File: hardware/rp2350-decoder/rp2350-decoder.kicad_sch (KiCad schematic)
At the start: 67 parts, among them J1 SWDIO, J2 SWCLK, J3 5052702412, Q1 DMN2991UDA-7B, Q2 DMN2991UDA-7B, Q3 NST847BPDP6T5G, Q4 NST847BPDP6T5G, Q5 DMN2991UDA-7B, Q6 DMN2991UDA-7B, Q7 DMN2991UDA-7B, Q8 DMN2991UDA-7B, SW1 BOOT, U1 NCS2220AMUT1G, U2 AP63203WU, U3 W25Q128JVPIQ, U4 RP2350A, U5 MAX98357AEWL+T, U6 MD9927, Y1 ABM8-272-T3

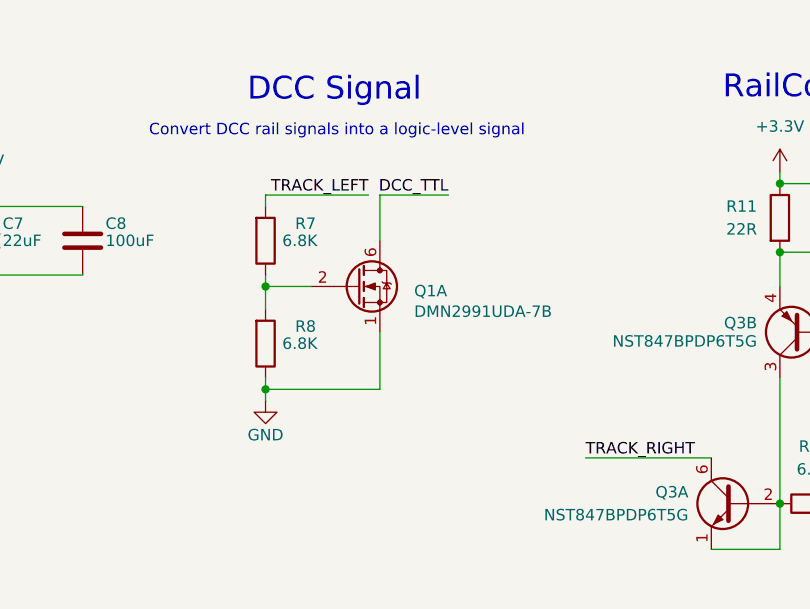
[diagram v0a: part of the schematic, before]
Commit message: fix: lower gate voltage to the dcc signal mosfet
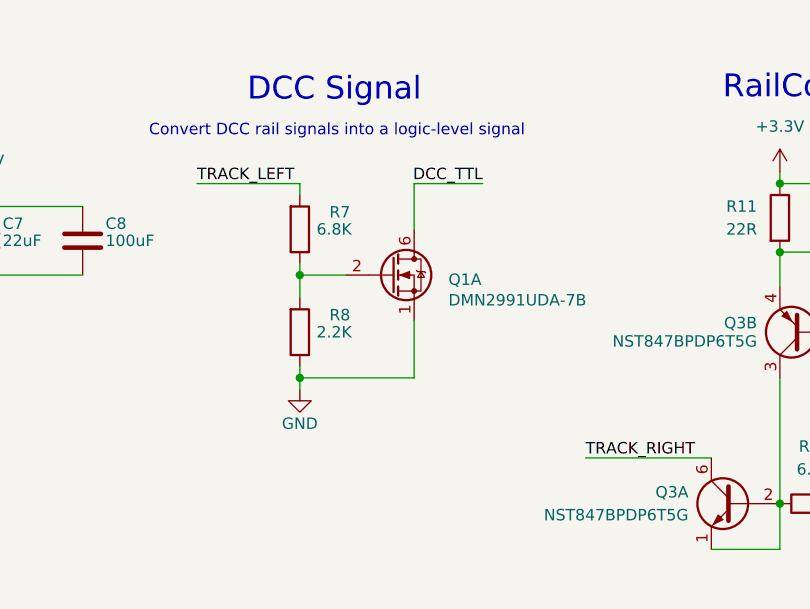
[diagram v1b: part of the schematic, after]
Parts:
- R8: value 6.8K -> 2.2K; LCSC C423451 -> C473534
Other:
- moved on the sheet: Q1A, R7, R8
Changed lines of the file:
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@@
 	)
 	(junction
-		(at 149.86 63.5)
+		(at 153.67 62.23)
 		(diameter 0)
 		(color 0 0 0 0)
@@
 	)
 	(junction
-		(at 149.86 52.07)
+		(at 153.67 50.8)
 		(diameter 0)
 		(color 0 0 0 0)
@@
 	(wire
 		(pts
-			(xy 149.86 50.8) (xy 149.86 52.07)
+			(xy 153.67 49.53) (xy 153.67 50.8)
 		)
 		(stroke
@@
 	(wire
 		(pts
-			(xy 162.56 57.15) (xy 162.56 63.5)
+			(xy 166.37 55.88) (xy 166.37 62.23)
 		)
 		(stroke
@@
 	(wire
 		(pts
-			(xy 149.86 41.91) (xy 149.86 43.18)
+			(xy 153.67 40.64) (xy 153.67 41.91)
 		)
 		(stroke
@@
 	(wire
 		(pts
-			(xy 149.86 62.23) (xy 149.86 63.5)
+			(xy 153.67 60.96) (xy 153.67 62.23)
 		)
 		(stroke
@@
 	(wire
 		(pts
-			(xy 162.56 41.91) (xy 170.18 41.91)
+			(xy 166.37 40.64) (xy 173.99 40.64)
 		)
 		(stroke
@@
 	(wire
 		(pts
-			(xy 149.86 52.07) (xy 149.86 54.61)
+			(xy 153.67 50.8) (xy 153.67 53.34)
 		)
 		(stroke
@@
 	(wire
 		(pts
-			(xy 149.86 63.5) (xy 162.56 63.5)
+			(xy 153.67 62.23) (xy 166.37 62.23)
 		)
 		(stroke
@@
 	(wire
 		(pts
-			(xy 162.56 41.91) (xy 162.56 46.99)
+			(xy 166.37 40.64) (xy 166.37 45.72)
 		)
 		(stroke
@@
 	(wire
 		(pts
-			(xy 149.86 52.07) (xy 154.94 52.07)
+			(xy 153.67 50.8) (xy 158.75 50.8)
 		)
 		(stroke
@@
 	(wire
 		(pts
-			(xy 161.29 41.91) (xy 149.86 41.91)
+			(xy 142.24 40.64) (xy 153.67 40.64)
 		)
 		(stroke
@@
 	(wire
 		(pts
-			(xy 149.86 64.77) (xy 149.86 63.5)
+			(xy 153.67 63.5) (xy 153.67 62.23)
 		)
 		(stroke
@@
 	)
 	(label "TRACK_LEFT"
-		(at 161.29 41.91 180)
+		(at 142.24 40.64 0)
 		(effects
 			(font
 				(size 1.27 1.27)
 			)
-			(justify right bottom)
+			(justify left bottom)
 		)
 	)
@@
 	)
 	(label "DCC_TTL"
-		(at 170.18 41.91 180)
+		(at 173.99 40.64 180)
 		(effects
 			(font
@@
 	(symbol
 		(lib_id "Device:R")
-		(at 149.86 58.42 0)
+		(at 153.67 57.15 0)
 		(mirror x)
 		(unit 1)
@@
 		(dnp no)
 		(property "Reference" "R8"
-			(at 154.305 56.515 0)
+			(at 158.115 55.245 0)
 			(effects
 				(font
@@
 			)
 		)
-		(property "Value" "6.8K"
-			(at 153.67 58.42 0)
+		(property "Value" "2.2K"
+			(at 157.48 57.15 0)
 			(effects
 				(font
@@
 		)
 		(property "Footprint" "Resistor_SMD:R_0201_0603Metric"
-			(at 148.082 58.42 90)
+			(at 151.892 57.15 90)
 			(effects
 				(font
@@
 		)
 		(property "Datasheet" "~"
-			(at 149.86 58.42 0)
+			(at 153.67 57.15 0)
 			(effects
 				(font
@@
 		)
 		(property "Description" ""
-			(at 149.86 58.42 0)
+			(at 153.67 57.15 0)
 			(effects
 				(font
@@
 		)
 		(property "Tolerance" "10%"
-			(at 153.67 60.325 0)
+			(at 157.48 59.055 0)
 			(effects
 				(font
@@
 			)
 		)
-		(property "LCSC" "C423451"
-			(at 149.86 58.42 0)
+		(property "LCSC" "C473534"
+			(at 153.67 57.15 0)
 			(effects
 				(font
@@
 		)
 		(property "Height" "0.26"
-			(at 149.86 58.42 0)
+			(at 153.67 57.15 0)
 			(effects
 				(font
@@
 		(lib_name "GND_1")
 		(lib_id "power:GND")
-		(at 149.86 64.77 0)
+		(at 153.67 63.5 0)
 		(unit 1)
 		(exclude_from_sim no)
@@
 		(dnp no)
 		(property "Reference" "#PWR023"
-			(at 149.86 71.12 0)
+			(at 153.67 69.85 0)
 			(effects
 				(font
@@
 		)
 		(property "Value" "GND"
-			(at 149.86 68.58 0)
+			(at 153.67 67.31 0)
 			(effects
 				(font
@@
 		)
 		(property "Footprint" ""
-			(at 149.86 64.77 0)
+			(at 153.67 63.5 0)
 			(effects
 				(font
@@
 		)
 		(property "Datasheet" ""
-			(at 149.86 64.77 0)
+			(at 153.67 63.5 0)
 			(effects
 				(font
@@
 		)
 		(property "Description" "Power symbol creates a global label with name \"GND\" , ground"
-			(at 149.86 64.77 0)
+			(at 153.67 63.5 0)
 			(effects
 				(font
@@
 	(symbol
 		(lib_id "rp2350-decoder:DMN2991UDA-7B")
-		(at 160.02 52.07 0)
+		(at 163.83 50.8 0)
 		(unit 1)
 		(exclude_from_sim no)
@@
 		(dnp no)
 		(property "Reference" "Q1"
-			(at 166.37 52.578 0)
+			(at 170.18 51.308 0)
 			(effects
 				(font
@@
 		)
 		(property "Value" "DMN2991UDA-7B"
-			(at 166.37 54.864 0)
+			(at 170.18 53.594 0)
 			(effects
 				(font
@@
 		)
 		(property "Footprint" "rp2350-decoder:X2-DFN0806-6_L0.8-W0.6_X2-DFN0806-6"
-			(at 165.1 53.975 0)
+			(at 168.91 52.705 0)
 			(effects
 				(font
@@
 		)
 		(property "Datasheet" "https://wmsc.lcsc.com/wmsc/upload/file/pdf/v2/lcsc/2201121800_Diodes-Incorporated-DMN2991UDA-7B_C2937136.pdf"
-			(at 165.1 55.88 0)
+			(at 168.91 54.61 0)
 			(effects
 				(font
@@
 		)
 		(property "Description" "20V 450mA 310mW 990mΩ@100mA,4.5V 1V@250uA 2 N-Channel X2-DFN0806-6 MOSFETs ROHS"
-			(at 160.02 65.278 0)
+			(at 163.83 64.008 0)
 			(effects
 				(font
@@
 		)
 		(property "LCSC" "C2937136"
-			(at 160.02 52.07 0)
+			(at 163.83 50.8 0)
 			(effects
 				(font
@@
 		)
 		(property "Height" "0.4"
-			(at 160.02 52.07 0)
+			(at 163.83 50.8 0)
 			(effects
 				(font
@@
 	(symbol
 		(lib_id "Device:R")
-		(at 149.86 46.99 0)
+		(at 153.67 45.72 0)
 		(mirror x)
 		(unit 1)
@@
 		(dnp no)
 		(property "Reference" "R7"
-			(at 154.305 45.085 0)
+			(at 158.115 43.815 0)
 			(effects
 				(font
@@
 		)
 		(property "Value" "6.8K"
-			(at 153.67 46.99 0)
+			(at 157.48 45.72 0)
 			(effects
 				(font
@@
 		)
 		(property "Footprint" "Resistor_SMD:R_0201_0603Metric"
-			(at 148.082 46.99 90)
+			(at 151.892 45.72 90)
 			(effects
 				(font
@@
 		)
 		(property "Datasheet" "~"
-			(at 149.86 46.99 0)
+			(at 153.67 45.72 0)
 			(effects
 				(font
@@
 		)
 		(property "Description" ""
-			(at 149.86 46.99 0)
+			(at 153.67 45.72 0)
 			(effects
 				(font
@@
 		)
 		(property "Tolerance" "10%"
-			(at 153.67 48.895 0)
+			(at 157.48 47.625 0)
 			(effects
 				(font
@@
 		)
 		(property "LCSC" "C423451"
-			(at 149.86 46.99 0)
+			(at 153.67 45.72 0)
 			(effects
 				(font
@@
 		)
 		(property "Height" "0.26"
-			(at 149.86 46.99 0)
+			(at 153.67 45.72 0)
 			(effects
 				(font
